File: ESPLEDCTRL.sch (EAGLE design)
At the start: 13 parts, among them IC1 74HC1G08GW, J1 22-27-2031-03, J2 22-27-2041-04, X3 ZX62D-B-5PA8, X4 MINI-USB-32005-201

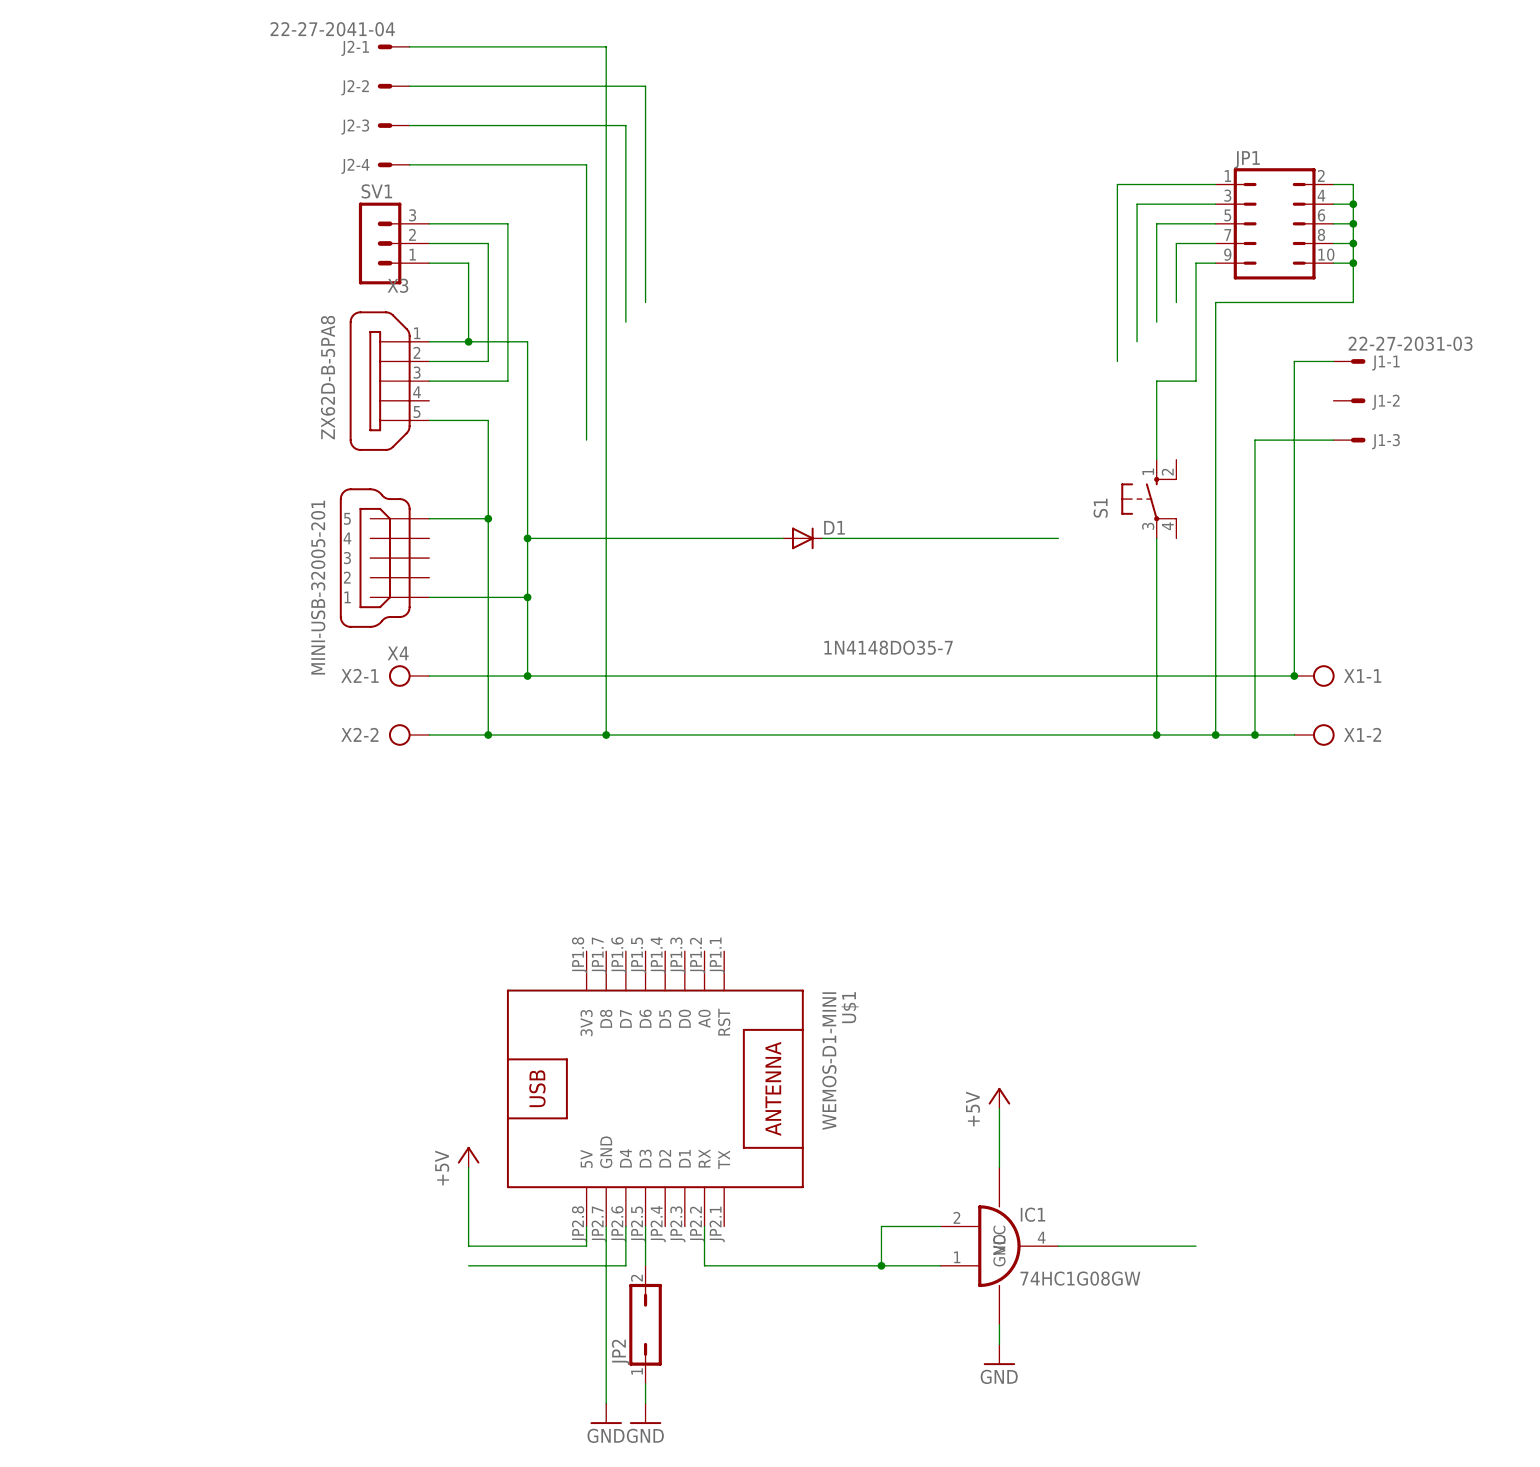
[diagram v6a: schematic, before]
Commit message: Leiterplatte Anordnung vorbereitet DCDC wandler ist 14mm hoch
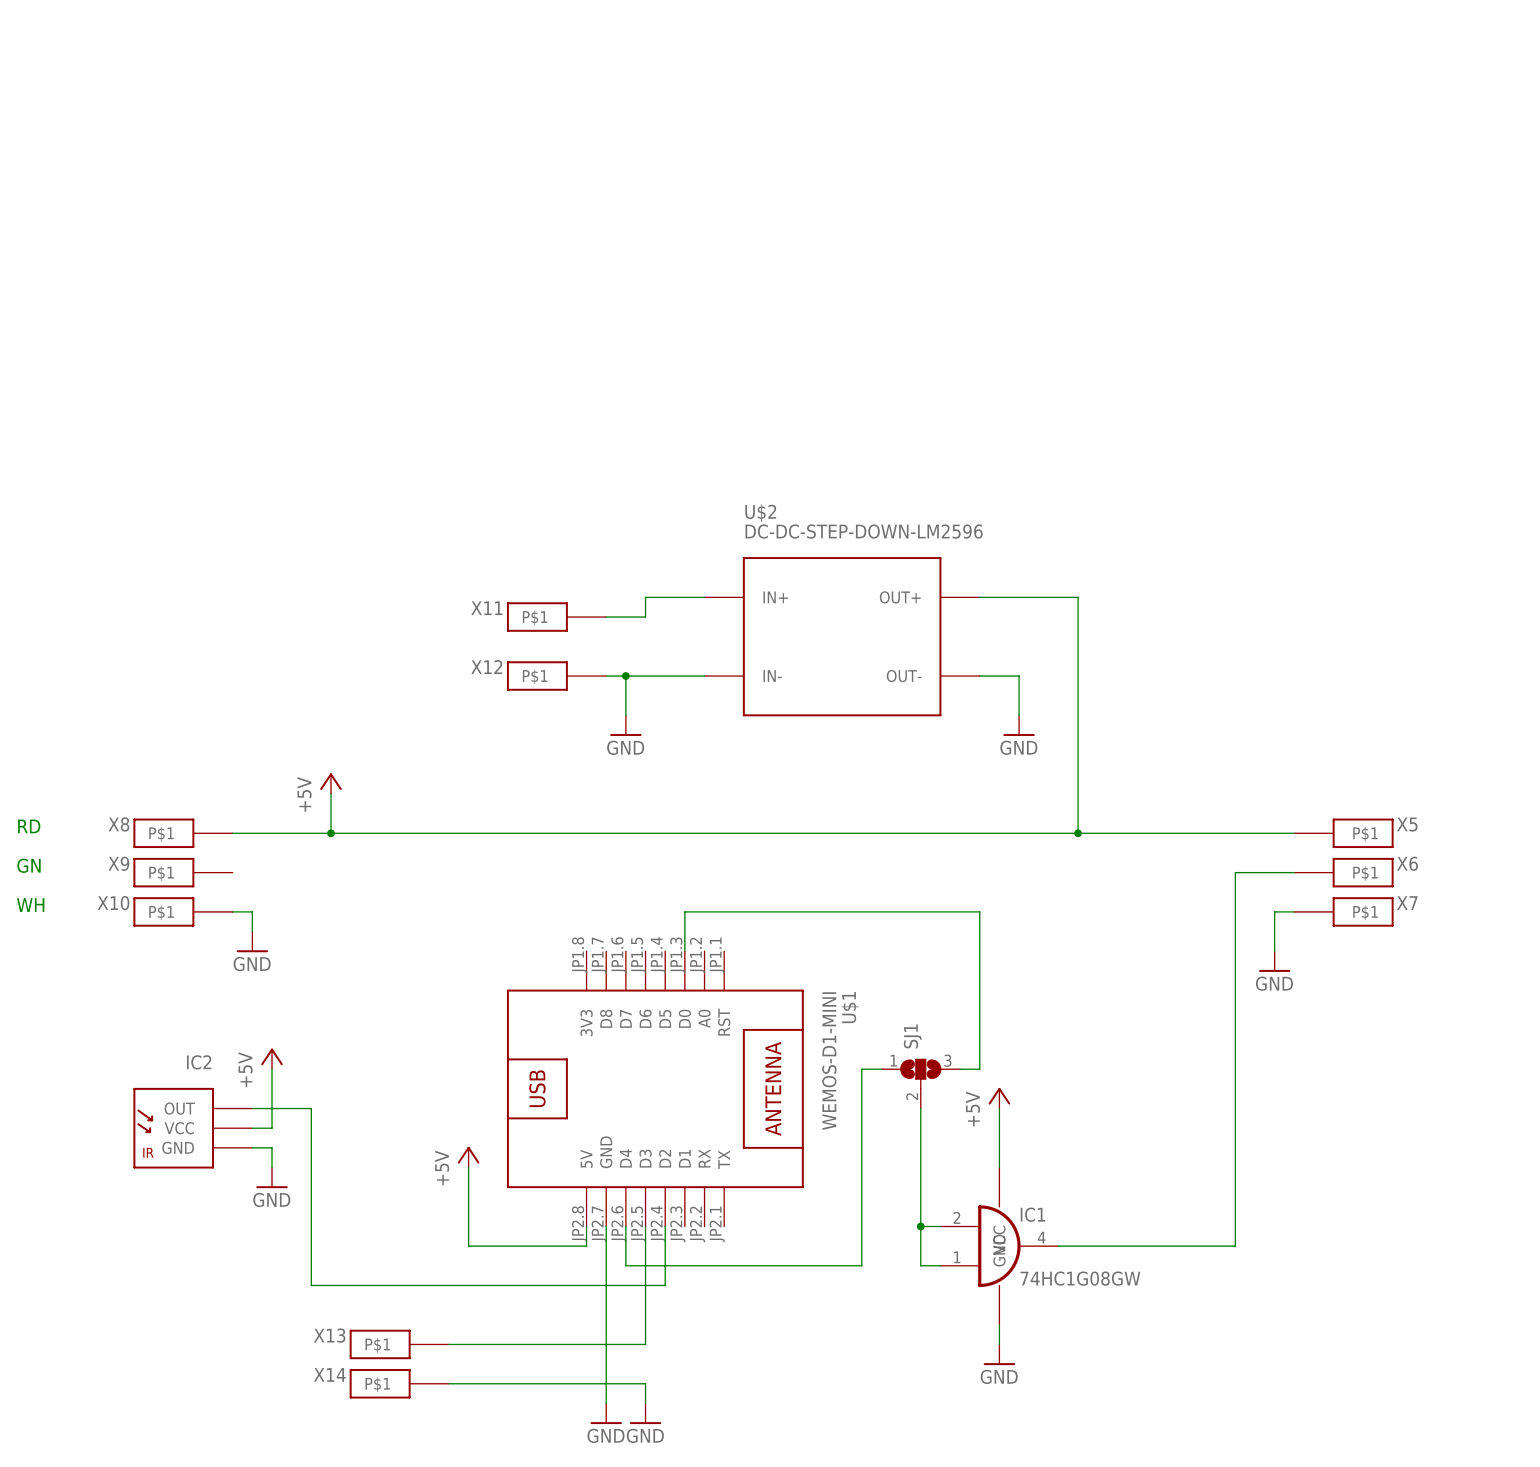
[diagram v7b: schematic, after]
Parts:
- removed D1: 1N4148DO35-7, diode:1N4148DO35-7
- removed J1: 22-27-2031-03, con-molex:22-27-2031-03
- removed J2: 22-27-2041-04, con-molex:22-27-2041-04
- removed JP1: (no value), jumper:JP5Q
- removed JP2: (no value), jumper:JP1Q
- removed S1: (no value), switch-omron:10-XX
- removed SV1: (no value), con-lstb:MA03-1
- removed X1, X2: (no value), con-ptr500:AK300/2
- removed X3: ZX62D-B-5PA8, zx62d-b-5pa8-oshpark_10:ZX62D-B-5PA8
- removed X4: MINI-USB-32005-201, con-cypressindustries:MINI-USB-32005-201
- added IC2: (no value), modules:TSOP382
- added SJ1: (no value), jumper:SJ2W
- added U$2: DC-DC-STEP-DOWN-LM2596, diy-modules:DC-DC-STEP-DOWN-LM2596
- added X10, X11, X12, X13, X14, X5, X6, X7, X8, X9: (no value), modules:PAD2X4
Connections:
- removed net N$10: J2-3.S
- removed net N$11: J1-3.S, J2-1.S, JP1.10, JP1.2, JP1.4, JP1.6, JP1.8, S1.P, X1-2.KL, X2-2.KL, X3G$1.5, X4.5
- removed net N$12: J2-4.S
- removed net N$13: D1.A, J1-1.S, SV1.1, X1-1.KL, X2-1.KL, X3G$1.1, X4.1
- removed net N$14: SV1.3, X3G$1.3
- removed net N$3: SV1.2, X3G$1.2
- removed net N$4: JP1.9, S1.S
- removed net N$5: JP1.1
- removed net N$6: J2-2.S
- removed net N$7: JP1.3
- removed net N$8: JP1.5
- removed net N$9: JP1.7
- new net N$17: SJ1.3, U$1.D0
- new net N$21: U$2.IN+, X11.P$1
- net +5V: now also IC2.VCC, U$2.OUT+, X5.P$1, X8.P$1
- net GND: now also IC2.GND, U$2.IN-, U$2.OUT-, X10.P$1, X12.P$1, X14.P$1, X7.P$1; no longer JP2.1
- net N$1: now also X13.P$1; no longer JP2.2
- net N$15: now also SJ1.1
- net N$16: now also SJ1.2; no longer U$1.RX
- net N$18: now also X6.P$1
- net N$2: now also IC2.OUT, U$1.D2; no longer D1.C
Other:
- note added: "GN"
- note added: "RD"
- note added: "WH"

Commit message: Board fertig gestellt
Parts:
- removed X9: (no value), modules:PAD2X4
- added C1, C2: (no value), rcl:C-EUC1206
- added C12: 100uF, rcl:CPOL-USD
- added D1: 1N5819-T, diode:1N5819-T
- added SJ2: (no value), jumper:SJ2W
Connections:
- removed net N$21: U$2.IN+, X11.P$1
- new net +12V: D1.C, SJ2.1, U$2.IN+, X11.P$1
- new net V+: SJ2.2, X5.P$1, X8.P$1
- net +5V: now also C1.1, C12.+, C2.1, D1.A, SJ2.3; no longer X5.P$1, X8.P$1
- net GND: now also C1.2, C12.-, C2.2
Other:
- note removed: "GN"
- moved on the sheet: U$2, X11, X12
